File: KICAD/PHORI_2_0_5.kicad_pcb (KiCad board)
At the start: 2 copper layers, 125 x 80.9 mm, 114 parts, among them J1 Conn_01x06_Female, J2 Conn_01x02, J2 Conn_01x04_Female, J4 Conn_01x01, J4 Conn_01x04_Male, J5 Rumble, J6 PinSocket_1x04_P2.00mm_Vertic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, J9 USB_B_Micro, Q1 Q_NMOS_GSD, Q2 Q_PMOS_GDS, Q3 Q_NMOS_GSD, SW1 A, SW10 Dup, SW11 Dright, SW2 B, SW4 Y, SW5 Start, SW6 L, SW7 R, SW8 Z, U1 MCP3002, U10 DRV5055Z3QDBZT, U11 DRV5055Z3QDBZT, U12 USBLC6-2P6, U13 USBLC6-2P6, U2 Stickbox_Assembly_Main, U3 DRV5055Z3QDBZT, U4 DRV5055Z3QDBZT, U5 Stickbox_Assembly, U6 AMS1117-3.3, U7 W25Q128JVS, U8 RP2040, Y1 Crystal_GND24

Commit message: fixed stick hole
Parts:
- removed ?: , 
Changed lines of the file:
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@@
     (pad "MP" thru_hole circle (at 3.5 2.5 24) (size 2.5 2.5) (drill 1.5) (layers "*.Cu" "*.Mask"))
-  )
-  (footprint "" (layer "F.Cu")
-    (at 105.639357 75.846441)
-    (fp_text reference "" (at 0 0) (layer "F.SilkS")
-        (effects (font (size 1.27 1.27) (thickness 0.15)))
-    )
-    (fp_text value "" (at 0 0) (layer "F.SilkS")
-        (effects (font (size 1.27 1.27) (thickness 0.15)))
-    )
-    (pad "" np_thru_hole circle (at 0 0) (size 1.8 1.8) (drill 1.8) (layers "F&B.Cu" "*.Mask"))
   )
   (footprint "PhobGCC_2_0_0_footprints:R_0603_1608Metric_Pad0.98x0.95mm_HandSolder" (layer "F.Cu")

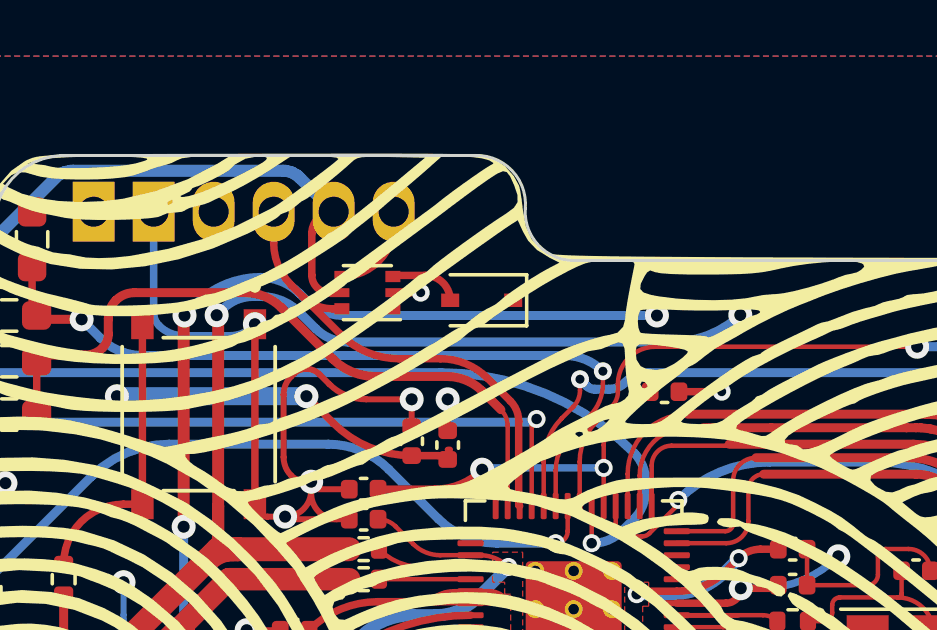
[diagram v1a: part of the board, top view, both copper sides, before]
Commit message: added d+- holes
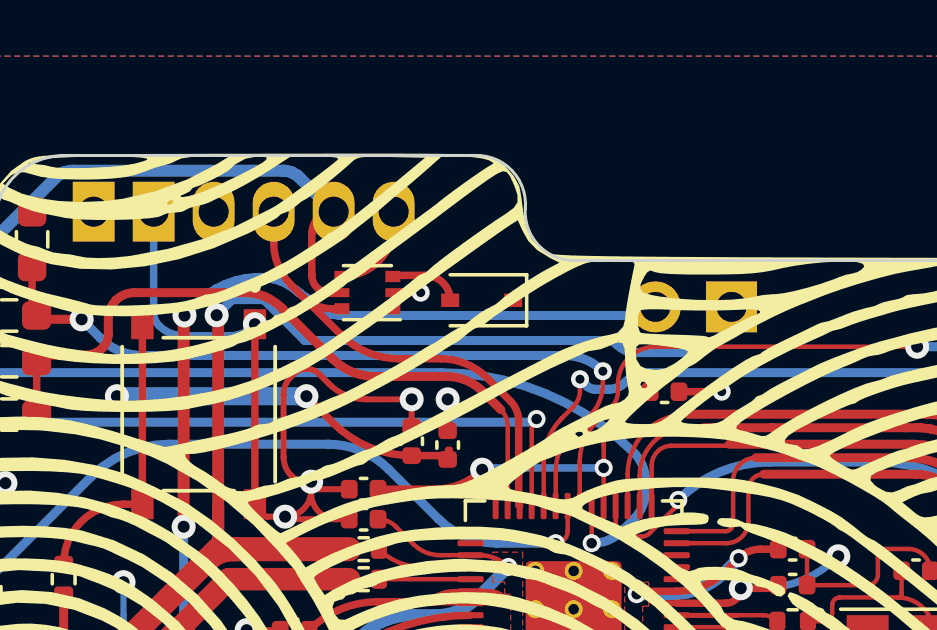
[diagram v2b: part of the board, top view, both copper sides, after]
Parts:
- added SW7: R, PhobGCC_Footprints:Pin_Header_Straight_1x02_Pitch2.54mm, B.Cu at (153.7, 54.1)
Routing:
- net USB_D+: track 87.3 -> 87.9 mm, vias 4 -> 3
- net USB_D-: track 87.5 -> 88.1 mm, vias 2 -> 1

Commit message: Updated CPL
Added updated CPL and Gerber for ordering at JLC
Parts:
- moved SW7 2.63 mm to (151.0, 54.0)
- moved SW6 2.12 mm to (95.3, 89.0)
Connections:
- J1 pad 1: (no net) -> +3V3
- U1 pad 1: (no net) -> CS1
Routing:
- net Net-(D2-Pad2): track 82.3 -> 59.4 mm, vias 2 -> 4
- net +3V3: track 76.6 -> 91.2 mm, vias 10 -> 20
- net GND: track 155.6 -> 162.4 mm, vias 45 -> 47
- net USB_D-: track 88.1 -> 86.1 mm
- net USB_D+: track 87.9 -> 86.1 mm
- net Ranalog: track 35.1 -> 34.0 mm
- net Rumble: track 28.7 -> 29.3 mm
- net L: track 85.3 -> 84.9 mm, vias 2 -> 1
- net (no net): vias 6 -> 1
